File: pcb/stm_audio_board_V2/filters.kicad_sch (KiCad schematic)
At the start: 31 parts

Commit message: added choke to analog pwr, created 5 V rail, decided to pivot and use codec instead dedicated hardware
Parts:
- removed C25, C26: 120p, Capacitor_SMD:C_0603_1608Metric_Pad1.08x0.95mm_HandSolder, symbol Device:C_Small
- removed C38: 5.6nF, Capacitor_SMD:C_0603_1608Metric_Pad1.08x0.95mm_HandSolder, symbol Device:C_Small
- removed C39: 390pF, Capacitor_SMD:C_0603_1608Metric_Pad1.08x0.95mm_HandSolder, symbol Device:C_Small
- removed R10: 5.76k, Resistor_SMD:R_0805_2012Metric_Pad1.20x1.40mm_HandSolder, symbol Device:R
- removed R12: 562, Resistor_SMD:R_0805_2012Metric_Pad1.20x1.40mm_HandSolder, symbol Device:R

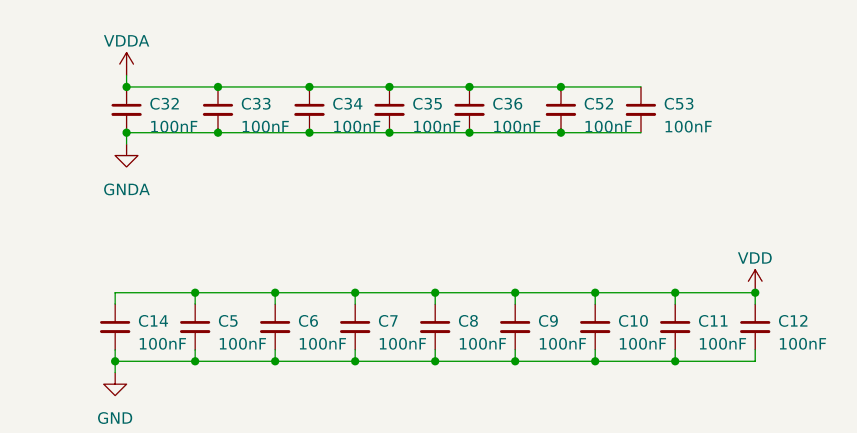
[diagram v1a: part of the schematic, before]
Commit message: ad1939 symbol is finished
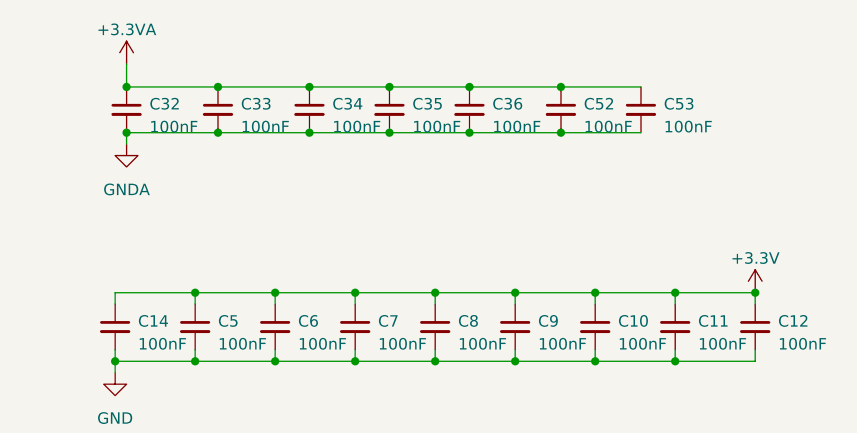
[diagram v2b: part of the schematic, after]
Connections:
- net VDD renamed +3.3V
- net VDDA renamed +3.3VA
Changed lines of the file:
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@@
     (stroke (width 0) (type default))
   )
-  (wire (pts (xy 26.67 26.67) (xy 26.67 27.94))
+  (wire (pts (xy 26.67 25.4) (xy 26.67 27.94))
     (stroke (width 0) (type default))
   )
@@
     )
   )
-  (symbol (lib_id "power:VDD") (at 96.52 50.8 0) (unit 1)
-    (in_bom yes) (on_board yes) (dnp no) (fields_autoplaced)
-    (property "Reference" "#PWR024" (at 96.52 54.61 0)
-      (effects (font (size 1.27 1.27)) hide)
-    )
-    (property "Value" "VDD" (at 96.52 46.99 0)
-      (effects (font (size 1.27 1.27)))
-    )
-    (property "Footprint" "" (at 96.52 50.8 0)
-      (effects (font (size 1.27 1.27)) hide)
-    )
-    (property "Datasheet" "" (at 96.52 50.8 0)
-      (effects (font (size 1.27 1.27)) hide)
-    )
-    (pin "1")
-    (instances
-      (project "stm_audio_board_V2"
-        (path "/6997cf63-2615-4e49-9471-e7da1b6bae71"
-          (reference "#PWR024") (unit 1)
-        )
-        (path "/6997cf63-2615-4e49-9471-e7da1b6bae71/927539c8-c0d0-4950-9b67-385a1cdd80f8"
-          (reference "#PWR024") (unit 1)
-        )
-      )
-    )
-  )
   (symbol (lib_id "Device:C_Small") (at 52.07 54.61 0) (unit 1)
     (in_bom yes) (on_board yes) (dnp no) (fields_autoplaced)
@@
         (path "/6997cf63-2615-4e49-9471-e7da1b6bae71/927539c8-c0d0-4950-9b67-385a1cdd80f8"
           (reference "C12") (unit 1)
-        )
-      )
-    )
-  )
-  (symbol (lib_id "power:VDDA") (at 26.67 26.67 0) (unit 1)
-    (in_bom yes) (on_board yes) (dnp no) (fields_autoplaced)
-    (property "Reference" "#PWR038" (at 26.67 30.48 0)
-      (effects (font (size 1.27 1.27)) hide)
-    )
-    (property "Value" "VDDA" (at 26.67 22.86 0)
-      (effects (font (size 1.27 1.27)))
-    )
-    (property "Footprint" "" (at 26.67 26.67 0)
-      (effects (font (size 1.27 1.27)) hide)
-    )
-    (property "Datasheet" "" (at 26.67 26.67 0)
-      (effects (font (size 1.27 1.27)) hide)
-    )
-    (pin "1")
-    (instances
-      (project "stm_audio_board_V2"
-        (path "/6997cf63-2615-4e49-9471-e7da1b6bae71"
-          (reference "#PWR038") (unit 1)
-        )
-        (path "/6997cf63-2615-4e49-9471-e7da1b6bae71/927539c8-c0d0-4950-9b67-385a1cdd80f8"
-          (reference "#PWR038") (unit 1)
         )
       )
@@
     )
   )
+  (symbol (lib_id "power:+3.3V") (at 96.52 50.8 0) (unit 1)
+    (in_bom yes) (on_board yes) (dnp no) (fields_autoplaced)
+    (property "Reference" "#PWR081" (at 96.52 54.61 0)
+      (effects (font (size 1.27 1.27)) hide)
+    )
+    (property "Value" "+3.3V" (at 96.52 46.99 0)
+      (effects (font (size 1.27 1.27)))
+    )
+    (property "Footprint" "" (at 96.52 50.8 0)
+      (effects (font (size 1.27 1.27)) hide)
+    )
+    (property "Datasheet" "" (at 96.52 50.8 0)
+      (effects (font (size 1.27 1.27)) hide)
+    )
+    (pin "1")
+    (instances
+      (project "stm_audio_board_V2"
+        (path "/6997cf63-2615-4e49-9471-e7da1b6bae71/2eb2ee8f-ab98-4666-97f0-bfacb073bc88"
+          (reference "#PWR081") (unit 1)
+        )
+        (path "/6997cf63-2615-4e49-9471-e7da1b6bae71/927539c8-c0d0-4950-9b67-385a1cdd80f8"
+          (reference "#PWR024") (unit 1)
+        )
+      )
+    )
+  )
   (symbol (lib_id "Device:C_Small") (at 26.67 123.19 0) (unit 1)
     (in_bom yes) (on_board yes) (dnp no) (fields_autoplaced)
@@
         )
       )
+    )
+  )
+  (symbol (lib_id "power:+3.3VA") (at 26.67 25.4 0) (unit 1)
+    (in_bom yes) (on_board yes) (dnp no) (fields_autoplaced)
+    (property "Reference" "#PWR055" (at 26.67 29.21 0)
+      (effects (font (size 1.27 1.27)) hide)
+    )
+    (property "Value" "+3.3VA" (at 26.67 21.59 0)
+      (effects (font (size 1.27 1.27)))
+    )
+    (property "Footprint" "" (at 26.67 25.4 0)
+      (effects (font (size 1.27 1.27)) hide)
+    )
+    (property "Datasheet" "" (at 26.67 25.4 0)
+      (effects (font (size 1.27 1.27)) hide)
+    )
+    (pin "1")
+    (instances
+      (project "stm_audio_board_V2"
+        (path "/6997cf63-2615-4e49-9471-e7da1b6bae71/2eb2ee8f-ab98-4666-97f0-bfacb073bc88"
+          (reference "#PWR055") (unit 1)
+        )
+        (path "/6997cf63-2615-4e49-9471-e7da1b6bae71/927539c8-c0d0-4950-9b67-385a1cdd80f8"
+          (reference "#PWR038") (unit 1)
+        )
+      )

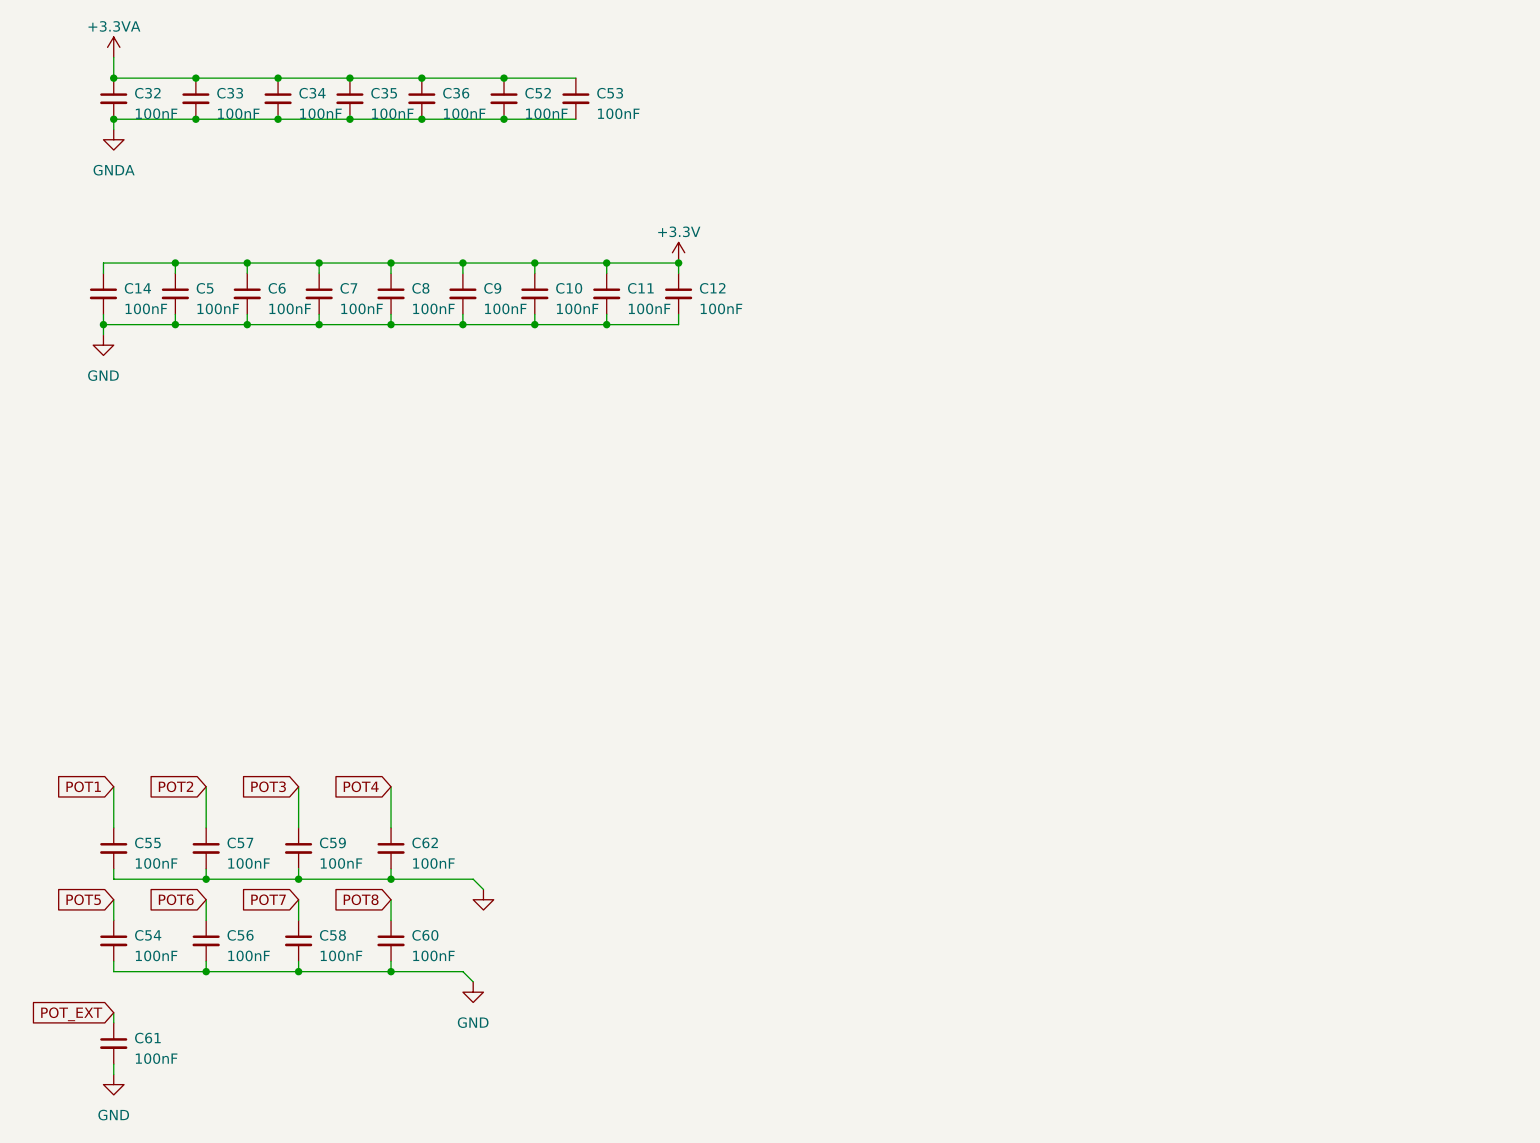
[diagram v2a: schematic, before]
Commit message: input and output stage reworked in sim and in schematic, power filtering is changed, further calculations needed
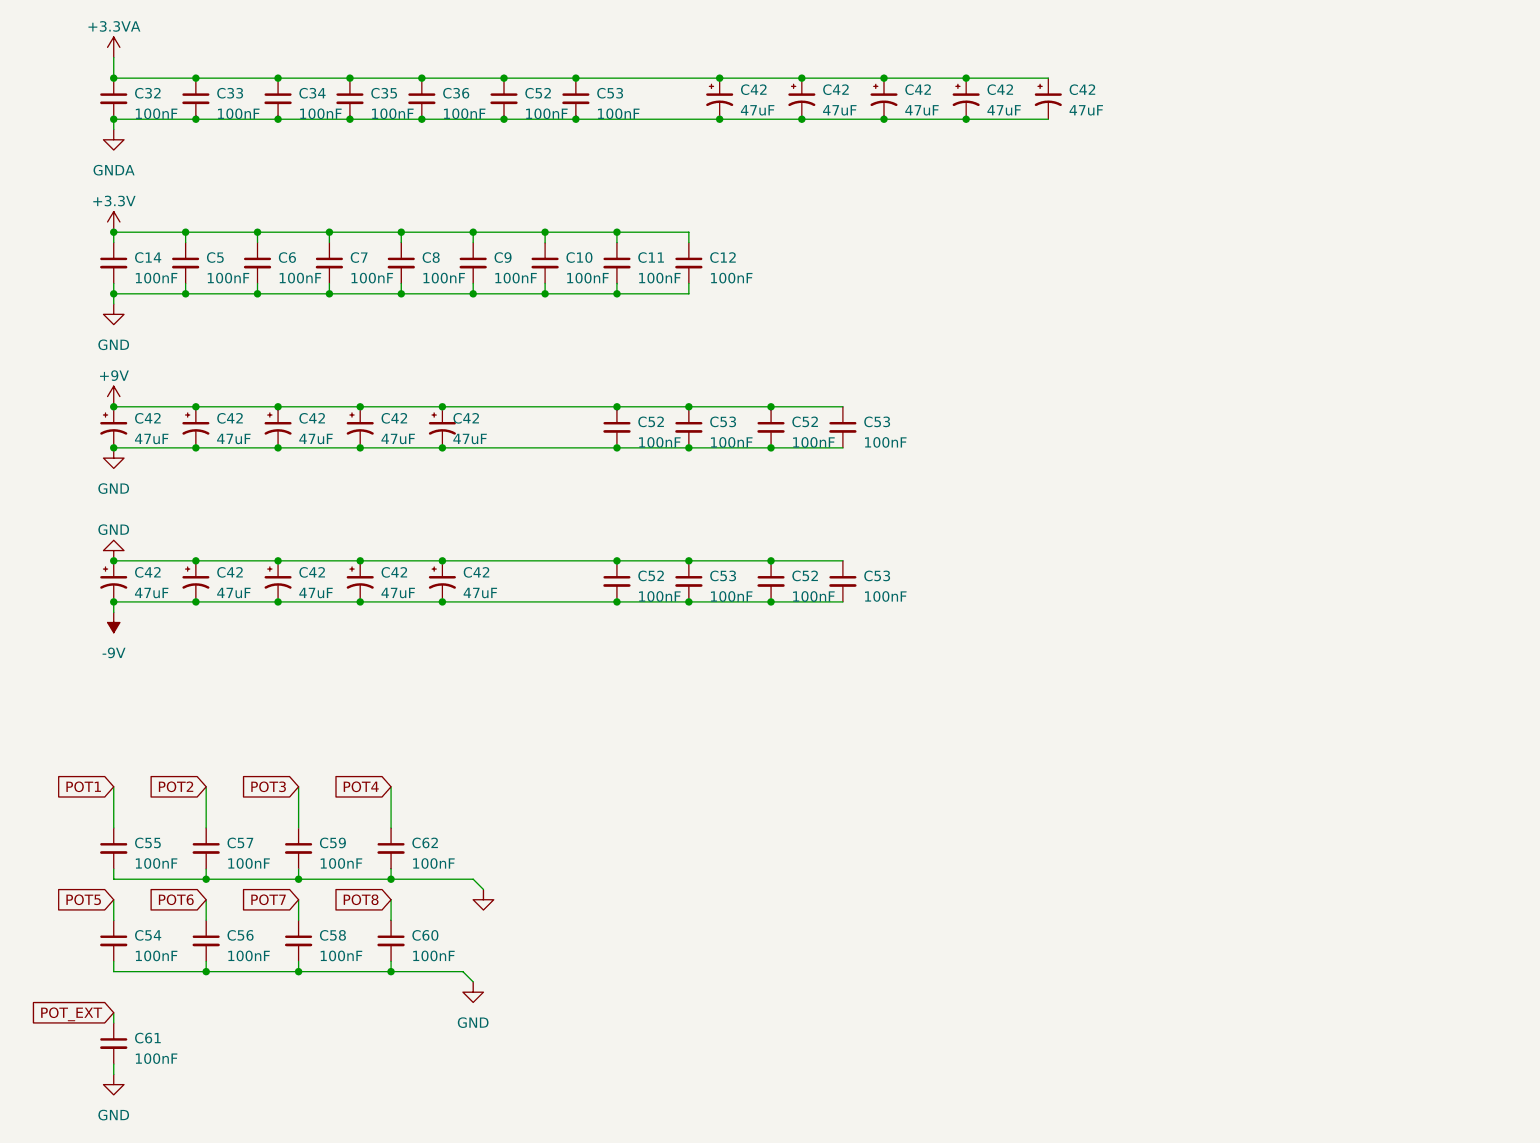
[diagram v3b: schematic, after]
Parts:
- added C42 (x15): 47uF, Capacitor_SMD:C_0805_2012Metric_Pad1.18x1.45mm_HandSolder, symbol Device:C_Polarized_Small_US
- added C52 (x4), C53 (x4): 100nF, Capacitor_SMD:C_0603_1608Metric_Pad1.08x0.95mm_HandSolder, symbol Device:C_Small
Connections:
- net +3.3VA: now also C42.1, C42.1, C42.1, C42.1, C42.1
- net GND: now also C42.1, C42.1, C42.1, C42.1, C42.1, C42.2, C42.2, C42.2, C42.2, C42.2, C52.1, C52.1, C52.2, C52.2, C53.1, C53.1, C53.2, C53.2
- net GNDA: now also C42.2, C42.2, C42.2, C42.2, C42.2
- new net +9V: C42.1, C42.1, C42.1, C42.1, C42.1, C52.1, C52.1, C53.1, C53.1
- new net -9V: C42.2, C42.2, C42.2, C42.2, C42.2, C52.2, C52.2, C53.2, C53.2
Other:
- moved on the sheet: C10, C11, C12, C14, C5, C6, C7, C8, C9

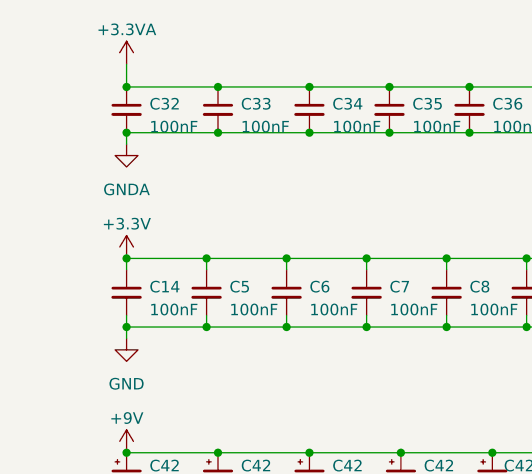
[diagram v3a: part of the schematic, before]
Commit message: PCB design started INPUT and OUTPUT stage done, codec placed
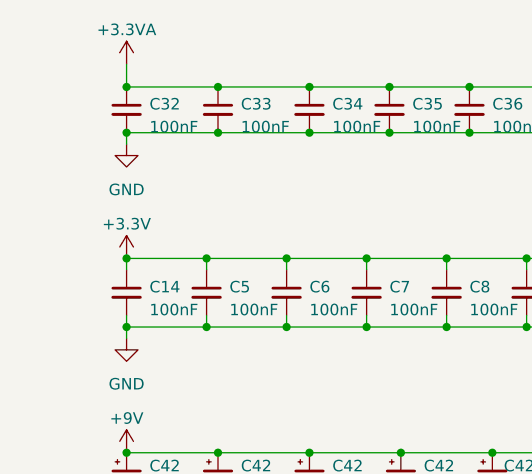
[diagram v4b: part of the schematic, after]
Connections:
- net GNDA is gone; now on net GND: C32.2, C33.2, C34.2, C35.2, C36.2, C42.2, C42.2, C42.2, C42.2, C42.2, C52.2, C53.2
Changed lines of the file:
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@@
+    )
+  )
+  (symbol (lib_id "power:GND") (at 26.67 34.29 0) (unit 1)
+    (in_bom yes) (on_board yes) (dnp no) (fields_autoplaced)
+    (property "Reference" "#PWR05" (at 26.67 40.64 0)
+      (effects (font (size 1.27 1.27)) hide)
+    )
+    (property "Value" "GND" (at 26.67 39.37 0)
+      (effects (font (size 1.27 1.27)))
+    )
+    (property "Footprint" "" (at 26.67 34.29 0)
+      (effects (font (size 1.27 1.27)) hide)
+    )
+    (property "Datasheet" "" (at 26.67 34.29 0)
+      (effects (font (size 1.27 1.27)) hide)
+    )
+    (pin "1")
+    (instances
+      (project "stm_audio_board_V2"
+        (path "/6997cf63-2615-4e49-9471-e7da1b6bae71"
+          (reference "#PWR05") (unit 1)
+        )
+        (path "/6997cf63-2615-4e49-9471-e7da1b6bae71/927539c8-c0d0-4950-9b67-385a1cdd80f8"
+          (reference "#PWR01") (unit 1)
+        )
+      )
     )
   )
@@
         )
       )
-    )
-  )
-  (symbol (lib_id "power:GNDA") (at 26.67 34.29 0) (unit 1)
-    (in_bom yes) (on_board yes) (dnp no) (fields_autoplaced)
-    (property "Reference" "#PWR039" (at 26.67 40.64 0)
-      (effects (font (size 1.27 1.27)) hide)
-    )
-    (property "Value" "GNDA" (at 26.67 39.37 0)
-      (effects (font (size 1.27 1.27)))
-    )
-    (property "Footprint" "" (at 26.67 34.29 0)
-      (effects (font (size 1.27 1.27)) hide)
-    )
-    (property "Datasheet" "" (at 26.67 34.29 0)
-      (effects (font (size 1.27 1.27)) hide)
-    )
-    (pin "1")
-    (instances
-      (project "stm_audio_board_V2"
-        (path "/6997cf63-2615-4e49-9471-e7da1b6bae71"
-          (reference "#PWR039") (unit 1)
-        )
-        (path "/6997cf63-2615-4e49-9471-e7da1b6bae71/927539c8-c0d0-4950-9b67-385a1cdd80f8"
-          (reference "#PWR039") (unit 1)
-        )
-      )
